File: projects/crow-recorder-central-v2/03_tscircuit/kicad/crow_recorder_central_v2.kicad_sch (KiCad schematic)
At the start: 194 parts, among them J1 C381116, J10 C9900035627, J2 C3020560, J3 C9900035627, J4 C9900035627, J5 C9900035627, J6 C9900035627, J7 C9900035627, J8 C9900035627, J9 C9900035627, Q1 C15127, Q2 C20917, U1 C6938291, U10 C6035451, U2 C181312, U3 C181312, U4 C232798, U5 C82317, U6 C2909890, U7 C5224055, U8 C5224055, U9 C150173, Y1 C7190380

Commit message: crow-recorder-central-v2 v1.0 source commit S: fresh-lens ORDER, its 2 P1s fixed at source, sourcing staged, twin gate green
Fresh zero-context integrated lens over the staged archive: VERDICT ORDER,
no P0, prior P0s verified repaired (08_reviews/2026-07-23_v1.0_fresh-lens
_integrated.md + DISPOSITIONS FL-*). Its two P1s FIXED pre-seal, not
deferred: CL1/CL2 22pF->12pF C0G C1547 (crystal CL 9pF; eff 14pF was
~30-50ppm of pull) and Cout_U10 1uF->2.2uF 25V X5R C72203 (Torex XC6227
phase-comp; the DETAIL_DESIGN '[PARTS confirm Cout]' placeholder finally
resolved). nets.yaml phantom PLUS5V_AUDIO replaced by the real P5VA_1..8
(measured 0.5mm x120 segments).

Sourcing at SOURCE (tsx supplierPartNumbers; 49-line BOM, every code ==
source): L1/L2 buck inductors (1277AS-H 2R2/1R0, sat-current qualified),
402k E96 for the uncatalogued 400k (-0.17% on 0V9), TLV70018 for
stock-zero TCR2LF18 (ADR-0006 fallback promoted), NX3225SA same-CL-9pF
for the stock-zero FA-238, and the WRONG-PART catch: BLM21PG600SN1D is a
60-ohm bead (Murata code 600 = 60R) — replaced by BLM21SP601SN1D
(600R/2.3A/60mR) in all 4 bead positions before any BOM shipped it.

Twin gate exit 0 (160 OK / 358; 8 evidence-backed adjudications incl. the
C99* consign RJ45 NO-CAD re-proven at 8 fetch attempts and the C464587
alternate-not-a-drop-in probe). CPL 172 (RJ45s + headers excluded,
pod-v2 pattern). Re-gated after every source edit: DRC 0/0/0,
check_port_nets 115/115 + 8/8, E-INV 7/7, count_parity 194x4, audit_board
21+11 (red-tested), policy_audit 0 FAIL exc M-REL (stamps at seal).
Ledgers harvested: proven-parts (beads/inductors/crystal + provenance
updates), lcsc_passives_ledger +8 catalog-verified codes.

Co-Authored-By: Claude Fable 5 <noreply@anthropic.com>
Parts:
- CL1, CL2: value 22pF -> 12pF
- Cout_U10: value 1uF -> 2.2uF
- R_fb2b: value 400kΩ -> 402kΩ
- U9: value C150173 -> C79924
- Y1: value C7190380 -> C2762192
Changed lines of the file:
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@@
   (symbol (lib_id "elt:SYM_R_fb2b") (at 499.110 240.030 0) (unit 1) (in_bom yes) (on_board yes) (dnp no)
     (property "Reference" "R_fb2b" (at 499.110 234.020 0) (effects (font (size 1.27 1.27))))
-    (property "Value" "400kΩ" (at 499.110 246.040 0) (effects (font (size 1.27 1.27))))
+    (property "Value" "402kΩ" (at 499.110 246.040 0) (effects (font (size 1.27 1.27))))
     (property "Footprint" "Resistor_SMD:R_0402_1005Metric" (at 499.110 240.030 0) (effects (font (size 1.27 1.27)) hide))
     (pin "1")
@@
   (symbol (lib_id "elt:SYM_U9") (at 94.615 237.490 0) (unit 1) (in_bom yes) (on_board yes) (dnp no)
     (property "Reference" "U9" (at 94.615 230.210 0) (effects (font (size 1.27 1.27))))
-    (property "Value" "C150173" (at 94.615 244.770 0) (effects (font (size 1.27 1.27))))
+    (property "Value" "C79924" (at 94.615 244.770 0) (effects (font (size 1.27 1.27))))
     (property "Footprint" "Package_TO_SOT_SMD:SOT-23-5" (at 94.615 237.490 0) (effects (font (size 1.27 1.27)) hide))
     (pin "1")
@@
   (symbol (lib_id "elt:SYM_Cout_U10") (at 500.380 267.335 0) (unit 1) (in_bom yes) (on_board yes) (dnp no)
     (property "Reference" "Cout_U10" (at 500.380 261.325 0) (effects (font (size 1.27 1.27))))
-    (property "Value" "1uF" (at 500.380 273.345 0) (effects (font (size 1.27 1.27))))
+    (property "Value" "2.2uF" (at 500.380 273.345 0) (effects (font (size 1.27 1.27))))
     (property "Footprint" "Capacitor_SMD:C_0402_1005Metric" (at 500.380 267.335 0) (effects (font (size 1.27 1.27)) hide))
     (pin "1")
@@
   (symbol (lib_id "elt:SYM_Y1") (at 94.615 271.780 0) (unit 1) (in_bom yes) (on_board yes) (dnp no)
     (property "Reference" "Y1" (at 94.615 265.770 0) (effects (font (size 1.27 1.27))))
-    (property "Value" "C7190380" (at 94.615 277.790 0) (effects (font (size 1.27 1.27))))
+    (property "Value" "C2762192" (at 94.615 277.790 0) (effects (font (size 1.27 1.27))))
     (property "Footprint" "Crystal:Crystal_SMD_SeikoEpson_FA238-4Pin_3.2x2.5mm" (at 94.615 271.780 0) (effects (font (size 1.27 1.27)) hide))
     (pin "1")
@@
   (symbol (lib_id "elt:SYM_CL1") (at 41.910 304.800 0) (unit 1) (in_bom yes) (on_board yes) (dnp no)
     (property "Reference" "CL1" (at 41.910 298.790 0) (effects (font (size 1.27 1.27))))
-    (property "Value" "22pF" (at 41.910 310.810 0) (effects (font (size 1.27 1.27))))
+    (property "Value" "12pF" (at 41.910 310.810 0) (effects (font (size 1.27 1.27))))
     (property "Footprint" "Capacitor_SMD:C_0402_1005Metric" (at 41.910 304.800 0) (effects (font (size 1.27 1.27)) hide))
     (pin "1")
@@
   (symbol (lib_id "elt:SYM_CL2") (at 40.640 233.680 0) (unit 1) (in_bom yes) (on_board yes) (dnp no)
     (property "Reference" "CL2" (at 40.640 227.670 0) (effects (font (size 1.27 1.27))))
-    (property "Value" "22pF" (at 40.640 239.690 0) (effects (font (size 1.27 1.27))))
+    (property "Value" "12pF" (at 40.640 239.690 0) (effects (font (size 1.27 1.27))))
     (property "Footprint" "Capacitor_SMD:C_0402_1005Metric" (at 40.640 233.680 0) (effects (font (size 1.27 1.27)) hide))
     (pin "1")

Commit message: crow-central v1.1 WIP checkpoint: F1+F2 source edits landed, reroute pending
F1: XU316 EP footprint's 16 duplicate-numbered 0.30/0.15 thru-hole pads
REMOVED (they emitted as ComponentDrill under the pasted EP); replaced by
03_src/add_u1_thermal_vias.py (stopgap per 03_src contract, promotion
schema in its docstring) which seeds 16 REAL GND via objects on the same
4x4 grid at rebuild step 3.5 + a --seal-fab-flags mode setting board
(capping yes)(filling yes) at step 4.5. audit_board grows a U1-EP
16-GND-vias gate.
F2: USB_DM renamed USB_DN everywhere (KiCad pairs nets only by P/N suffix
— DP/DM never matched, so no diff-pair rule could fire); nets.yaml
USB_DIFF class with diff_pair {0.125/0.15} solved for JLC06161H-3313
(prepreg 3313 h=0.0994 Er=4.1; 2D FD field solve 89.7-90.5 ohm);
audit_board grows the R-LEN skew<=1mm/width/F.Cu-only measurement gate.

KNOWN RED AT THIS CHECKPOINT: the regenerated converter schematic FAILS
check_port_nets (P5VA_4->AUDIO4M + MID2P label-lost — the v1.0 P0 merge
class is back in the FRESH tscircuit render; investigating whether the
v1.0 dogleg fix lived in the tsx or only in the committed kicad_sch).
Committed as a checkpoint, not a gate pass.

Co-Authored-By: Claude Fable 5 <noreply@anthropic.com>
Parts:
- FB_BEEP, FB_u18, FB_u33, L_pll: value simple_inductor -> C3716677
- L1: value simple_inductor -> C882626
- L2: value simple_inductor -> C237284
- Y1: footprint Crystal:Crystal_SMD_SeikoEpson_FA238-4Pin_3.2x2.5mm -> (none)
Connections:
- net MID2P is gone; now on net 5V: Cc2P.2, Rs2P.1
- net P5VA_4 is gone; now on net AUDIO4M: F4.2, J6.4, J6.7
- net GND: now also J10.SH (SHIELD), J2.SH (SHIELD), J3.SH (SHIELD), J4.SH (SHIELD), J5.SH (SHIELD), J6.SH (SHIELD), J7.SH (SHIELD), J8.SH (SHIELD), J9.SH (SHIELD)
- net USB_DM renamed USB_DN

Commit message: crow-central v1.1: F1+F2 implemented, routing gate GREEN 0/0/0 from committed source
F1 (U1 EP via-in-pad): footprint thru-pads removed; rebuild step 3.5 seeds
16 REAL GND 0.30/0.15 vias on the 4x4 EP grid; step 4.5 sets board setup
(capping yes)(filling yes). MEASURED: PTH drill now emits NO 0.15
ComponentDrill tool at all — T1 ViaDrill 0.150 carries all 639 vias incl.
the 16 EP holes at (90,102)+/-{0.55,1.65}; remaining ComponentDrill tools
are real THT (0.6/0.89/1.0/1.57). audit_board gains the U1-EP 16-GND-via
gate.

F2 (USB HS 90ohm): promoted converter sch guarded in rebuild_all (the P0
dogleg surgery is a promoted artifact — a fresh converter render measurably
reintroduces the P5VA_4/MID2P merge class, check_port_nets RED); USB_DM ->
USB_DN rename (KiCad pairs only P/N suffixes); USB_DIFF netclass
diff_pair {w 0.125, gap 0.15} solved for JLC06161H-3313 (2D FD field
solve 89.7-90.5 ohm, sanity 50.6 ohm SE at w0.14); KRT route_diff reroute:
pair coupled at 0.155mm centers-gap measured, all F.Cu, 0 vias, lengths
DP 23.62 / DN 23.51, spread 0.110mm <= 1mm; chain re-promoted.
ACTIVATION PROOF (a gate that cannot fail is worthless): tightening the
dru min to 0.30mm produced 10 diff_pair_gap_out_of_range violations on a
board copy — the rule fires on this exact pair; restored rule re-gates
0/0/0. check_port_nets 115/115 + 8/8 re-verified after reroute.

Co-Authored-By: Claude Fable 5 <noreply@anthropic.com>
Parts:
- FB_BEEP, FB_u18, FB_u33, L_pll: value C3716677 -> simple_inductor
- L1: value C882626 -> simple_inductor
- L2: value C237284 -> simple_inductor
- Y1: footprint (none) -> Crystal:Crystal_SMD_SeikoEpson_FA238-4Pin_3.2x2.5mm
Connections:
- net 5V: no longer Cc2P.2, Rs2P.1
- net AUDIO4M: no longer F4.2, J6.4, J6.7
- net GND: no longer J10.SH (SHIELD), J2.SH (SHIELD), J3.SH (SHIELD), J4.SH (SHIELD), J5.SH (SHIELD), J6.SH (SHIELD), J7.SH (SHIELD), J8.SH (SHIELD), J9.SH (SHIELD)
- new net MID2P: Cc2P.2, Rs2P.1
- new net P5VA_4: F4.2, J6.4, J6.7

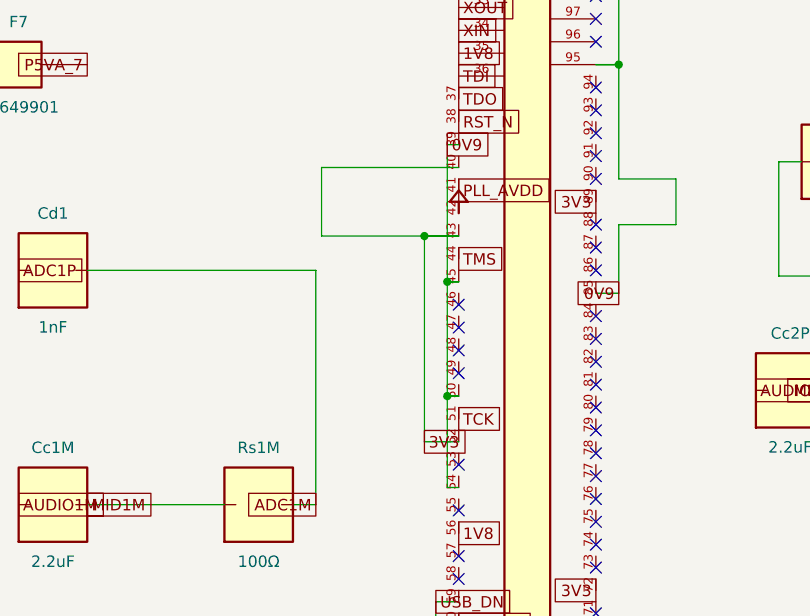
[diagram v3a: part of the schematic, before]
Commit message: crow-central v1.1: LV straps floated (PR2-P0-1 fix) + re-gate green, pre-lens checkpoint
U1.40/43/52 3V3 tie removed at source (tsx + promoted-sch surgery: 14
wires + 1 label excised — BFS-proven self-contained branch — + 3
no_connect markers = the ds v2.0.0 sec 4.8 float select); chain surgery
removed exactly 7 copper items (3 in-pad 3V3 vias + 4 dead segments; a
first graph-prune attempt over-deleted 9 zone/T-anchored segments and was
reverted from git before redoing as an explicit list). part.yaml strap
facts corrected (HIGH = IOB 1.8V, never 3V3).

Re-gate MEASURED: DRC 0/0/0 (+ staged-archive standalone 0/0/0); parity 0
(588 nodes / 146 no-connects both sides); ERC 0 err / 1201 warn (-14 =
excised branch); check_port_nets 115/115 + 8/8; audit_board green (USB
spread 0.110mm, U1-EP 16 GND vias); twin exit 0 (160 OK/359); BOM source
PASS vs the staged dir; v1.0-relative netlist diff = EXACTLY 7 node moves
(4x USB_DM->USB_DN + 3x LV to unconnected) — 06_build/verify/
lv_strap_fix_diff.md. Pin + render reviews archived verbatim in
08_reviews/ (both PASS; pin review's LV finding escalated, datasheet-
confirmed, fixed). Staged v1.1 dir refreshed to the fixed bytes; MANIFEST
still unstamped (seal step 2 pending fresh lens).

Co-Authored-By: Claude Fable 5 <noreply@anthropic.com>
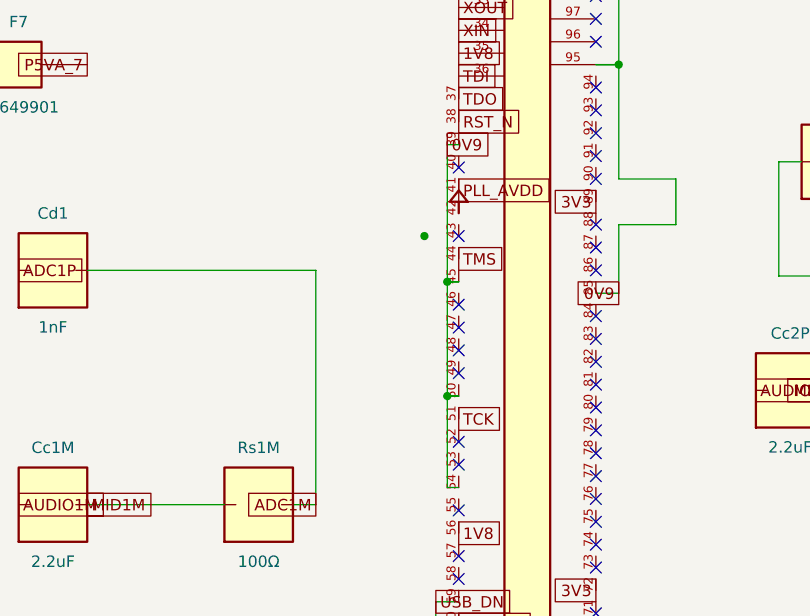
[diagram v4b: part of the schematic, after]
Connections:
- net 3V3: no longer U1.40, U1.43, U1.52
- no-connect marks 143 -> 146
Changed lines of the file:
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@@
   (global_label "3V3" (shape passive) (at 84.455 240.030 0) (fields_autoplaced) (effects (font (size 1.27 1.27)) (justify left)))
   (global_label "3V3" (shape passive) (at 198.120 244.475 0) (fields_autoplaced) (effects (font (size 1.27 1.27)) (justify left)))
-  (global_label "3V3" (shape passive) (at 198.120 333.375 0) (fields_autoplaced) (effects (font (size 1.27 1.27)) (justify left)))
   (global_label "3V3" (shape passive) (at 217.170 349.885 180) (fields_autoplaced) (effects (font (size 1.27 1.27)) (justify right)))
   (global_label "3V3" (shape passive) (at 217.170 306.705 180) (fields_autoplaced) (effects (font (size 1.27 1.27)) (justify right)))
@@
   (wire (pts (xy 217.805 238.125) (xy 217.805 225.425)) (stroke (width 0) (type default)))
   (wire (pts (xy 217.805 225.425) (xy 217.170 225.425)) (stroke (width 0) (type default)))
-  (wire (pts (xy 201.930 310.515) (xy 200.660 310.515)) (stroke (width 0) (type default)))
-  (wire (pts (xy 200.660 310.515) (xy 200.025 310.515)) (stroke (width 0) (type default)))
-  (wire (pts (xy 200.025 310.515) (xy 186.690 310.515)) (stroke (width 0) (type default)))
-  (wire (pts (xy 186.690 310.515) (xy 186.690 302.895)) (stroke (width 0) (type default)))
-  (wire (pts (xy 186.690 302.895) (xy 200.025 302.895)) (stroke (width 0) (type default)))
-  (wire (pts (xy 200.025 302.895) (xy 200.660 302.895)) (stroke (width 0) (type default)))
-  (wire (pts (xy 200.660 302.895) (xy 201.930 302.895)) (stroke (width 0) (type default)))
-  (wire (pts (xy 201.930 333.375) (xy 200.660 333.375)) (stroke (width 0) (type default)))
-  (wire (pts (xy 200.660 333.375) (xy 200.025 333.375)) (stroke (width 0) (type default)))
-  (wire (pts (xy 200.025 333.375) (xy 198.120 333.375)) (stroke (width 0) (type default)))
-  (wire (pts (xy 198.120 333.375) (xy 198.120 310.515)) (stroke (width 0) (type default)))
-  (wire (pts (xy 198.120 310.515) (xy 200.025 310.515)) (stroke (width 0) (type default)))
-  (wire (pts (xy 200.025 310.515) (xy 200.660 310.515)) (stroke (width 0) (type default)))
-  (wire (pts (xy 200.660 310.515) (xy 201.930 310.515)) (stroke (width 0) (type default)))
   (wire (pts (xy 217.170 245.745) (xy 217.805 245.745)) (stroke (width 0) (type default)))
   (wire (pts (xy 217.805 245.745) (xy 218.440 245.745)) (stroke (width 0) (type default)))
@@
   (no_connect (at 341.630 387.350))
   (no_connect (at 341.630 389.890))
+  (no_connect (at 201.930 302.895))
+  (no_connect (at 201.930 310.515))
+  (no_connect (at 201.930 333.375))
   (symbol (lib_id "elt:GND") (at 356.870 391.160 90) (unit 1) (in_bom no) (on_board yes) (dnp no)
     (property "Reference" "#PWR142" (at 356.870 391.160 0) (effects (font (size 1.27 1.27)) hide))
